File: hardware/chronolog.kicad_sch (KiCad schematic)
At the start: 0 parts

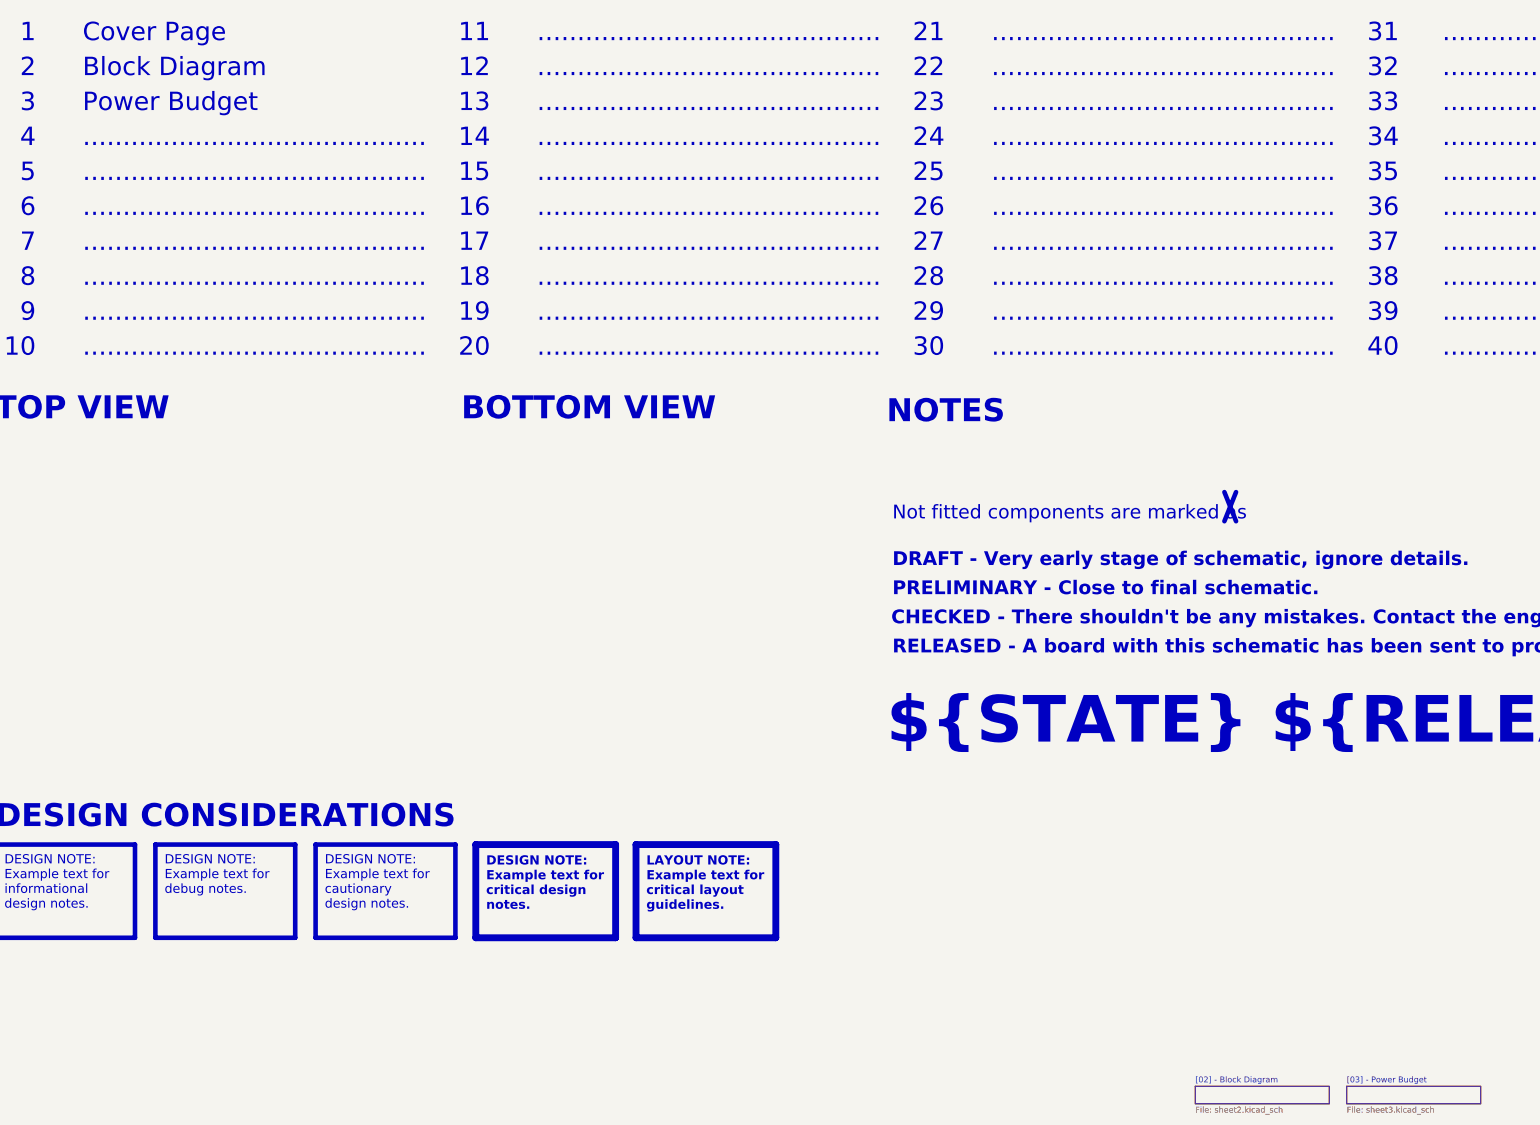
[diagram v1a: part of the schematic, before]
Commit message: hardware(feat): change power budget to power supply
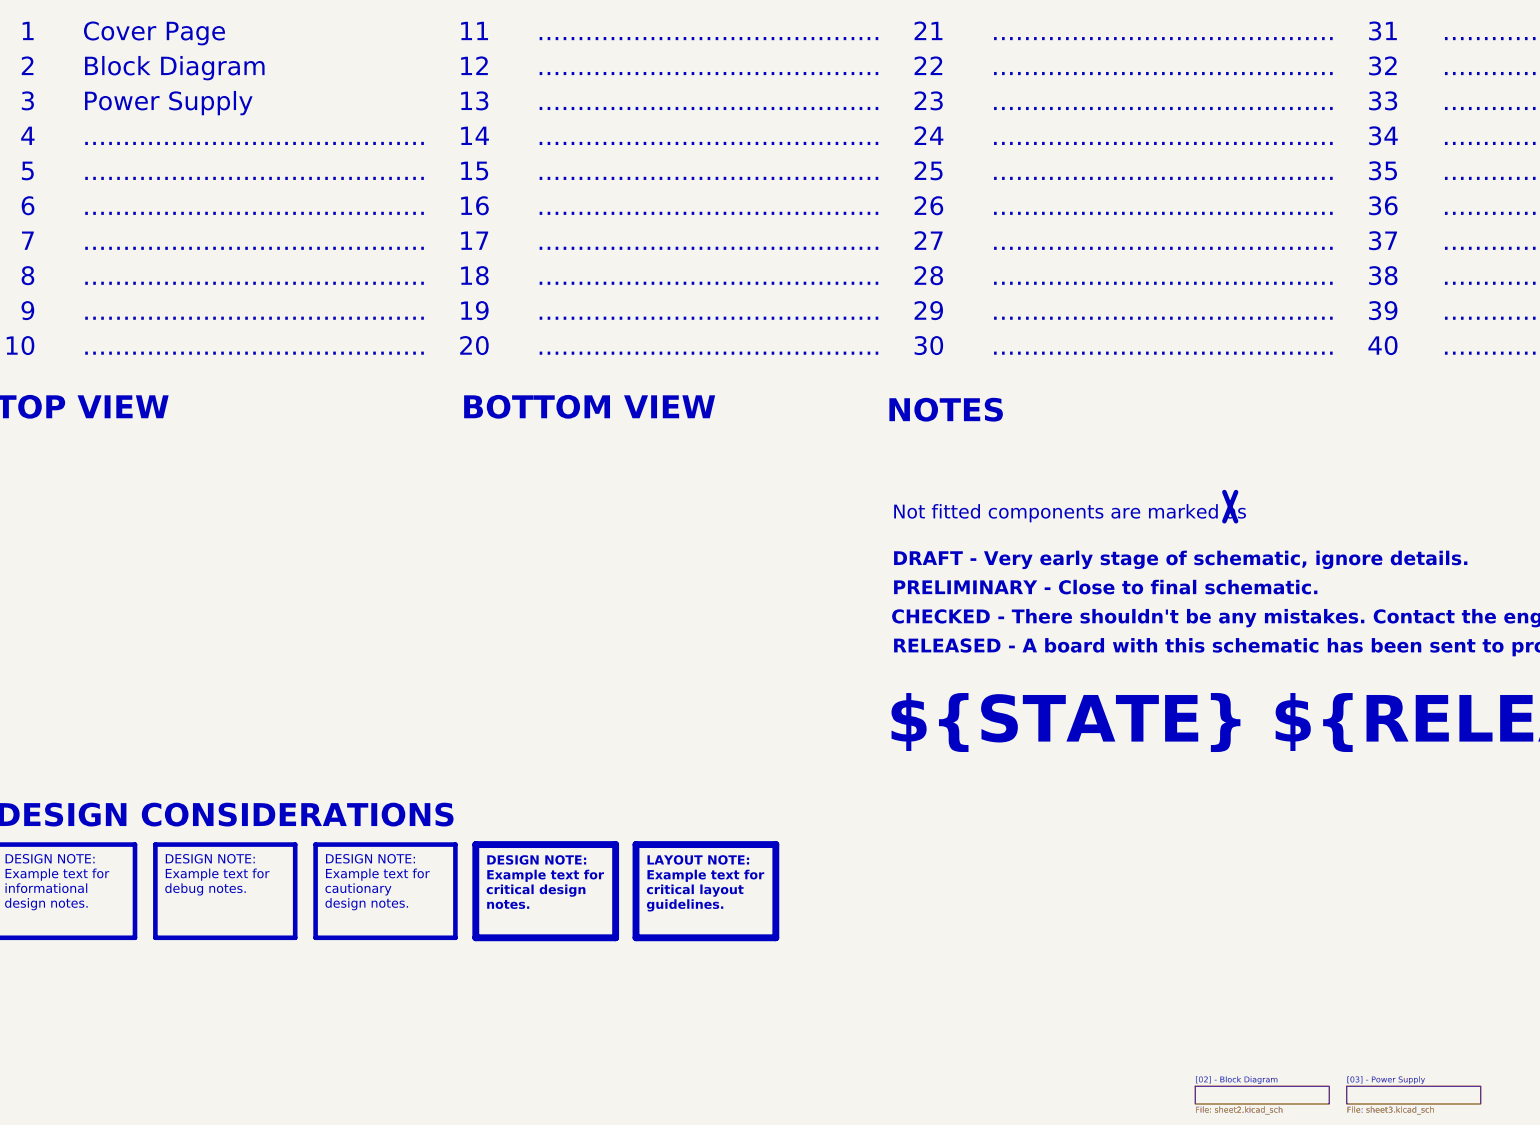
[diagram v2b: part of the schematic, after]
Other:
- sheet [03] - Power Budget renamed [03] - Power Supply
- note added: "Power Supply"
- note removed: "Power Budget"
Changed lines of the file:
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@@
 		)
 	)
-	(text "Power Budget"
+	(text "Power Supply"
 		(exclude_from_sim no)
 		(at 44.45 95.25 0)
@@
 			(color 0 0 0 0.0000)
 		)
-		(property "Sheetname" "[03] - Power Budget"
+		(property "Sheetname" "[03] - Power Supply"
 			(at 320.04 306.6284 0)
 			(effects

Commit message: hardware(feat): add mcu
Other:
- added sheet [04] - MCU (sheet4.kicad_sch)
- note added: "MCU"
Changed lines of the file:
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@@
 		)
 	)
-	(text "..........................................."
+	(text "MCU"
 		(exclude_from_sim no)
 		(at 44.45 102.87 0)
@@
 				)
 			)
+		)
+	)
+	(sheet
+		(at 353.06 307.34)
+		(size 29.21 3.81)
+		(exclude_from_sim no)
+		(in_bom yes)
+		(on_board yes)
+		(dnp no)
+		(fields_autoplaced yes)
+		(stroke
+			(width 0.1524)
+			(type solid)
+			(color 132 0 0 1)
+		)
+		(fill
+			(color 0 0 0 0.0000)
+		)
+		(property "Sheetname" "[04] - MCU"
+			(at 353.06 306.6284 0)
+			(effects
+				(font
+					(size 1.27 1.27)
+				)
+				(justify left bottom)
+			)
+		)
+		(property "Sheetfile" "sheet4.kicad_sch"
+			(at 353.06 311.7346 0)
+			(effects
+				(font
+					(size 1.27 1.27)
+				)
+				(justify left top)
+			)
+		)
+		(instances
+			(project "chronolog"
+				(path "/08767502-fa14-4976-aaca-9650785a2144"
+					(page "4")
+				)
+			)

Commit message: hardware(feat): add rtc battery and lse crystal (#2)
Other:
- added sheet [05] - RTC and NOR (sheet5.kicad_sch)
- note added: "RTC and NOR"
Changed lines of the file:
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@@
 		)
 	)
-	(text "..........................................."
+	(text "RTC and NOR"
 		(exclude_from_sim no)
 		(at 44.45 110.49 0)
@@
 				)
 			)
+		)
+	)
+	(sheet
+		(at 386.08 307.34)
+		(size 29.21 3.81)
+		(exclude_from_sim no)
+		(in_bom yes)
+		(on_board yes)
+		(dnp no)
+		(fields_autoplaced yes)
+		(stroke
+			(width 0.1524)
+			(type solid)
+			(color 132 0 0 1)
+		)
+		(fill
+			(color 0 0 0 0.0000)
+		)
+		(property "Sheetname" "[05] - RTC and NOR"
+			(at 386.08 306.6284 0)
+			(effects
+				(font
+					(size 1.27 1.27)
+				)
+				(justify left bottom)
+			)
+		)
+		(property "Sheetfile" "sheet5.kicad_sch"
+			(at 386.08 311.7346 0)
+			(effects
+				(font
+					(size 1.27 1.27)
+				)
+				(justify left top)
+			)
+		)
+		(instances
+			(project "chronolog"
+				(path "/08767502-fa14-4976-aaca-9650785a2144"
+					(page "5")
+				)
+			)

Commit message: hardware(feat): add push buttons with pull-ups and debounce (#3)
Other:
- added sheet [06] - Buttons and Sensors (sheet6.kicad_sch)
- note added: "Buttons and Sensors"
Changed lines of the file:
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@@
 		)
 	)
-	(text "..........................................."
+	(text "Buttons and Sensors"
 		(exclude_from_sim no)
 		(at 44.45 118.11 0)
@@
 				)
 			)
+		)
+	)
+	(sheet
+		(at 287.02 318.77)
+		(size 29.21 3.81)
+		(exclude_from_sim no)
+		(in_bom yes)
+		(on_board yes)
+		(dnp no)
+		(fields_autoplaced yes)
+		(stroke
+			(width 0.1524)
+			(type solid)
+		)
+		(fill
+			(color 0 0 0 0.0000)
+		)
+		(property "Sheetname" "[06] - Buttons and Sensors"
+			(at 287.02 318.0584 0)
+			(effects
+				(font
+					(size 1.27 1.27)
+				)
+				(justify left bottom)
+			)
+		)
+		(property "Sheetfile" "sheet6.kicad_sch"
+			(at 287.02 323.1646 0)
+			(effects
+				(font
+					(size 1.27 1.27)
+				)
+				(justify left top)
+			)
+		)
+		(instances
+			(project "chronolog"
+				(path "/08767502-fa14-4976-aaca-9650785a2144"
+					(page "6")
+				)
+			)

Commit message: hardware(feat): add esp-01 wifi module on usart3
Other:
- added sheet [07] - ESP-01 (sheet7.kicad_sch)
- note added: "ESP-01"
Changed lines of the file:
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@@
 		)
 	)
-	(text "..........................................."
+	(text "ESP-01"
 		(exclude_from_sim no)
 		(at 44.45 125.73 0)
@@
 				)
 			)
+		)
+	)
+	(sheet
+		(at 320.04 318.77)
+		(size 29.21 3.81)
+		(exclude_from_sim no)
+		(in_bom yes)
+		(on_board yes)
+		(dnp no)
+		(fields_autoplaced yes)
+		(stroke
+			(width 0.1524)
+			(type solid)
+		)
+		(fill
+			(color 0 0 0 0.0000)
+		)
+		(property "Sheetname" "[07] - ESP-01"
+			(at 320.04 318.0584 0)
+			(effects
+				(font
+					(size 1.27 1.27)
+				)
+				(justify left bottom)
+			)
+		)
+		(property "Sheetfile" "sheet7.kicad_sch"
+			(at 320.04 323.1646 0)
+			(effects
+				(font
+					(size 1.27 1.27)
+				)
+				(justify left top)
+			)
+		)
+		(instances
+			(project "chronolog"
+				(path "/08767502-fa14-4976-aaca-9650785a2144"
+					(page "7")
+				)
+			)
